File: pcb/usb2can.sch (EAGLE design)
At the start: 18 parts, among them IC1 ADM3053M, IC2 LD117AS33TR, K1 61400416021, K2 61900419521

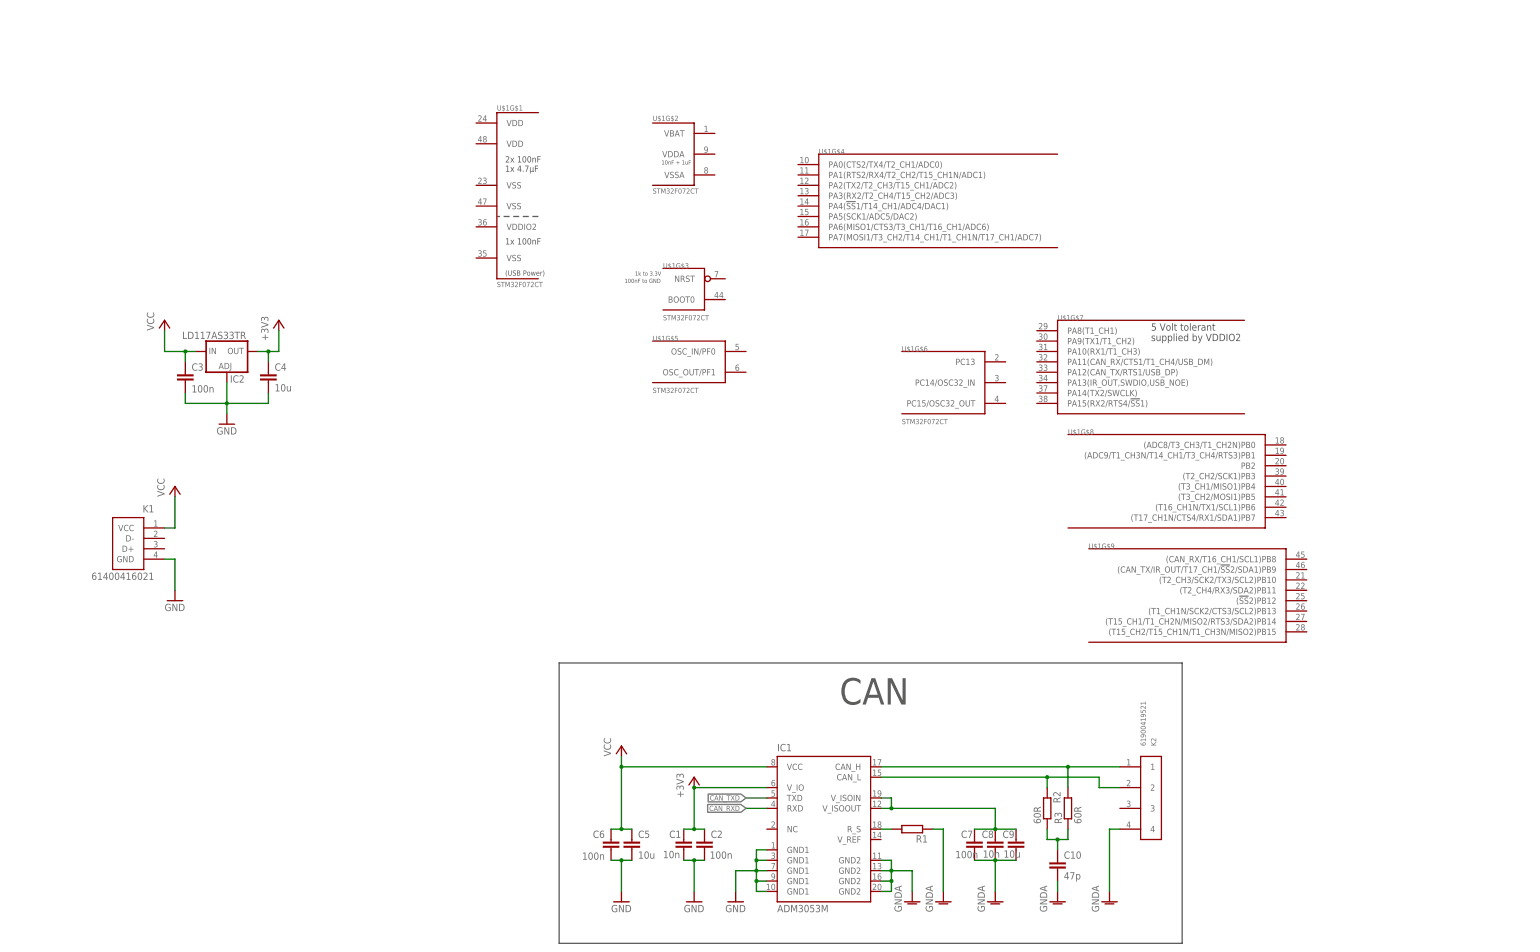
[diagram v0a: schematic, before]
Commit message: add some capacitors and connect USB and CAN
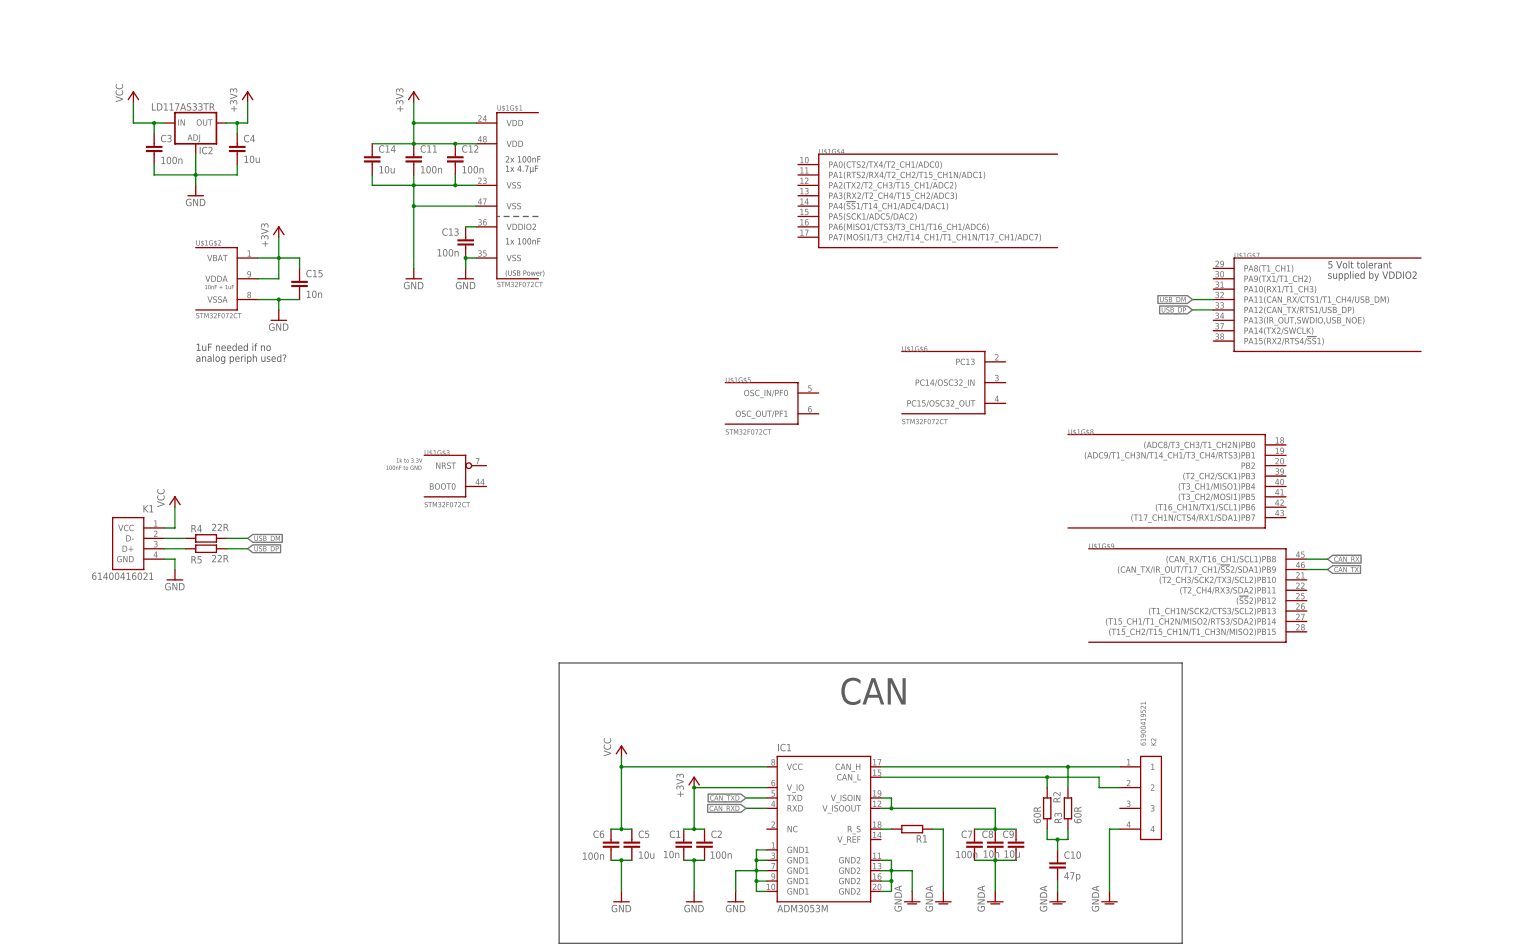
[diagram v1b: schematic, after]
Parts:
- added C11, C12, C13: 100n, rcl:C-EUC0603
- added C14: 10u, rcl:C-EUC0805K
- added C15: 10n, rcl:C-EUC0603
- added R4, R5: 22R, rcl:R-EU_R0805
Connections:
- new net CAN_RX: U$1G$9.(CAN_RX/T16_CH1/SCL1)PB8
- new net CAN_TX: U$1G$9.(CAN_TX/IR_OUT/T17_CH1/!SS!2/SDA1)PB9
- new net N$5: K1.D-, R4.1
- new net N$6: K1.D+, R5.1
- new net N$7: C13.1, U$1G$1.VDDIO2
- new net USB_DM: R4.2, U$1G$7.PA11(CAN_RX/CTS1/T1_CH4/USB_DM)
- new net USB_DP: R5.2, U$1G$7.PA12(CAN_TX/RTS1/USB_DP)
- net +3V3: now also C11.1, C12.1, C14.1, C15.1, U$1G$1.VDD@1, U$1G$1.VDD@2, U$1G$2.VBAT, U$1G$2.VDDA
- net GND: now also C11.2, C12.2, C13.2, C14.2, C15.2, U$1G$1.VSS@1, U$1G$1.VSS@2, U$1G$1.VSS@3, U$1G$2.VSSA
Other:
- note added: "1uF needed if no analog periph used?"
- moved on the sheet: C3, C4, IC2, U$1G$2, U$1G$3, U$1G$5, U$1G$7

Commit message: schematic: clock done, USB needs no series-R, debug port done, power supply revised
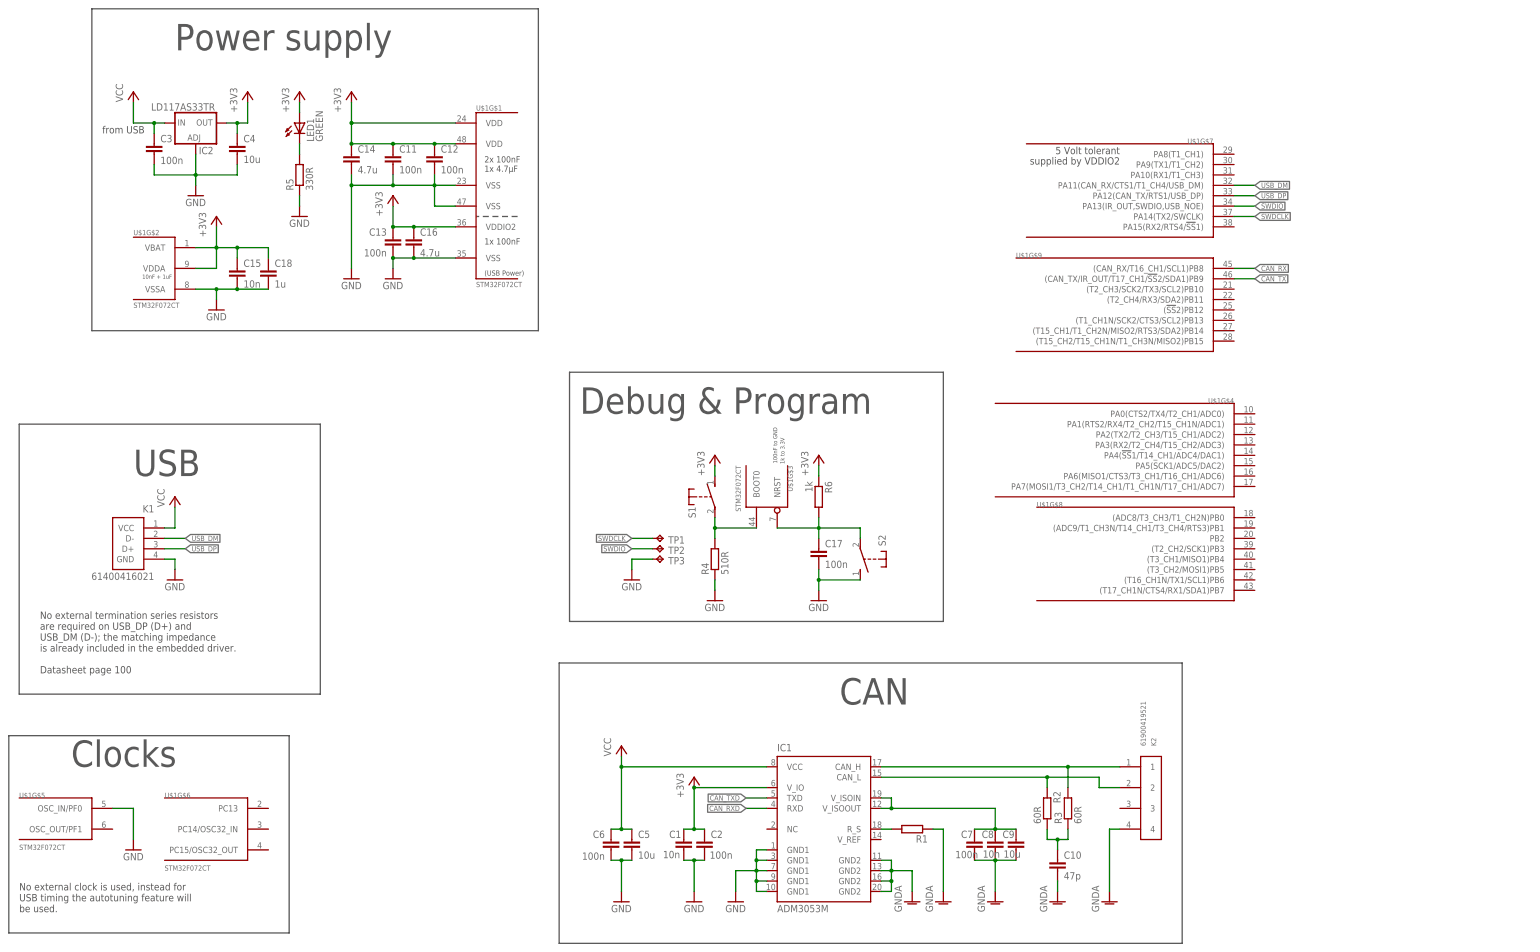
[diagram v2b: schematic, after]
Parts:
- added C16: 4.7u, rcl:C-EUC0805K
- added C17: 100n, rcl:C-EUC0603
- added C18: 1u, rcl:C-EUC0805K
- added LED1: GREEN, led:LEDCHIPLED_0603
- added R6: 1k, resistor:R-EU_R0603
- added S1, S2: MICRO_SWITCH_3X6X2.5S, micro_switch:MICRO_SWITCH_3X6X2.5S
- added TP1, TP2, TP3: TPB2,54, testpad:TPB2,54
- C14: value 10u -> 4.7u
- R4: value 22R -> 510R; device rcl:R-EU_R0805 -> resistor:R-EU_R0603
- R5: value 22R -> 330R; device rcl:R-EU_R0805 -> resistor:R-EU_R0603
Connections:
- new net SWDCLK: TP1.TP, U$1G$7.PA14(TX2/SWCLK)
- new net SWDIO: TP2.TP, U$1G$7.PA13(IR_OUT,SWDIO,USB_NOE)
- net +3V3: now also C13.1, C16.1, C18.1, LED1.A, R6.1, S1.1, U$1G$1.VDDIO2
- net GND: now also C16.2, C17.2, C18.2, R4.1, R5.1, S2.1, TP3.TP, U$1G$5.OSC_IN/PF0
- net N$5: now also LED1.C, R5.2; no longer K1.D-, R4.1
- net N$6: now also R4.2, S1.2, U$1G$3.BOOT0; no longer K1.D+, R5.1
- net N$7: now also C17.1, R6.2, S2.2, U$1G$3.NRST; no longer C13.1, U$1G$1.VDDIO2
- net USB_DM: now also K1.D-; no longer R4.2
- net USB_DP: now also K1.D+; no longer R5.2
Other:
- note added: "Clocks"
- note added: "Debug & Program"
- note added: "No external clock is used, instead for USB timing the autotuning feature will be used."
- note added: "No external termination series resistors are required on USB_DP (D+) and USB_DM (D-); the matching impedance is already included in the embedded driver. Datasheet page 100"
- note added: "Power supply"
- note added: "USB"
- note added: "from USB"
- note removed: "1uF needed if no analog periph used?"
- moved on the sheet: C11, C12, C13, C14, C15, R4, R5, U$1G$1, U$1G$2, U$1G$3, U$1G$4, U$1G$5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

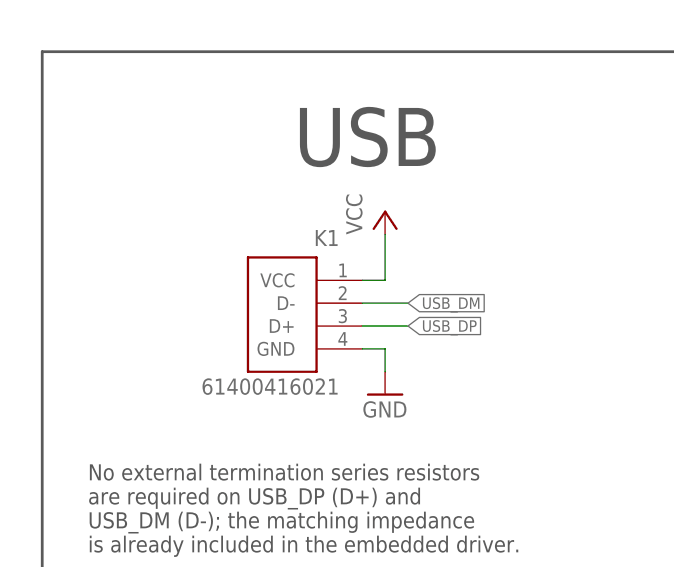
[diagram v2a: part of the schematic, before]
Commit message: schematic: use another usb connector and add forgotten library
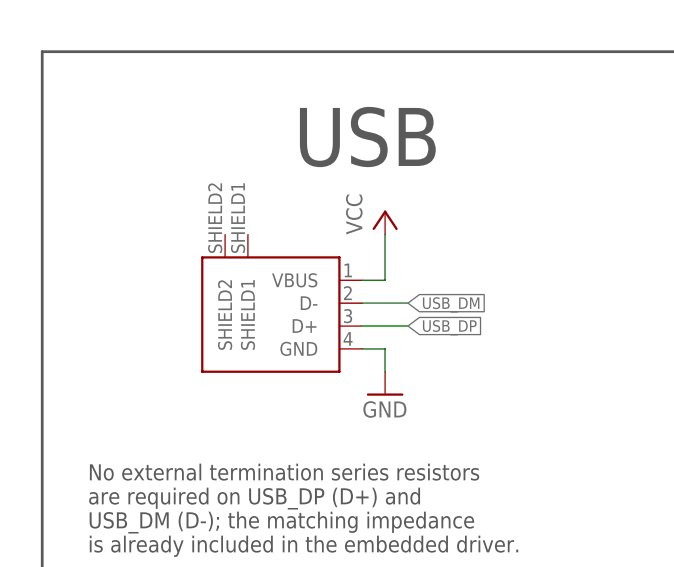
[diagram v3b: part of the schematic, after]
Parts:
- removed K1: 61400416021, Wuerth_Elektronik_eiCan_Communication_Connectors:61400416021
- added CON1: USB_A_MALESMD, micro_switch:USB_A_MALESMD
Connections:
- net GND: now also CON1.GND; no longer K1.GND
- net USB_DM: now also CON1.D-; no longer K1.D-
- net USB_DP: now also CON1.D+; no longer K1.D+
- net VCC: now also CON1.VBUS; no longer K1.VCC
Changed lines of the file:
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@@
 <part name="IC1" library="ADM3053" deviceset="ADM3053" device="M"/>
 <part name="GND1" library="supply1" deviceset="GND" device=""/>
-<part name="K1" library="Wuerth_Elektronik_eiCan_Communication_Connectors" deviceset="61400416021" device=""/>
 <part name="P+1" library="supply1" deviceset="VCC" device=""/>
 <part name="C1" library="rcl" deviceset="C-EU" device="C0603K" value="10n"/>
@@
 <part name="R5" library="resistor" deviceset="R-EU_" device="R0603" value="330R"/>
 <part name="GND18" library="supply1" deviceset="GND" device=""/>
+<part name="CON1" library="micro_switch" deviceset="USB_A_MALE" device="SMD"/>
 </parts>
 <sheets>
@@
 <instance part="IC1" gate="G$1" x="106.68" y="7.62"/>
 <instance part="GND1" gate="1" x="-53.34" y="68.58"/>
-<instance part="K1" gate="G$1" x="-66.04" y="78.74" rot="MR0"/>
 <instance part="P+1" gate="VCC" x="-53.34" y="88.9"/>
 <instance part="C1" gate="G$1" x="71.12" y="5.08" smashed="yes">
@@
 <instance part="R5" gate="G$1" x="-22.86" y="167.64" rot="R90"/>
 <instance part="GND18" gate="1" x="-22.86" y="157.48"/>
+<instance part="CON1" gate="G$1" x="-66.04" y="78.74"/>
 </instances>
 <busses>
@@
 <net name="VCC" class="0">
 <segment>
-<pinref part="K1" gate="G$1" pin="VCC"/>
 <wire x1="-55.88" y1="81.28" x2="-53.34" y2="81.28" width="0.1524" layer="91"/>
 <wire x1="-53.34" y1="81.28" x2="-53.34" y2="86.36" width="0.1524" layer="91"/>
 <pinref part="P+1" gate="VCC" pin="VCC"/>
+<pinref part="CON1" gate="G$1" pin="VBUS"/>
 </segment>
 <segment>
@@
 <net name="GND" class="0">
 <segment>
-<pinref part="K1" gate="G$1" pin="GND"/>
 <wire x1="-55.88" y1="73.66" x2="-53.34" y2="73.66" width="0.1524" layer="91"/>
 <wire x1="-53.34" y1="73.66" x2="-53.34" y2="71.12" width="0.1524" layer="91"/>
 <pinref part="GND1" gate="1" pin="GND"/>
+<pinref part="CON1" gate="G$1" pin="GND"/>
 </segment>
 <segment>
@@
 <segment>
 <label x="-50.8" y="78.74" size="1.27" layer="95" xref="yes"/>
-<pinref part="K1" gate="G$1" pin="D-"/>
 <wire x1="-55.88" y1="78.74" x2="-50.8" y2="78.74" width="0.1524" layer="91"/>
+<pinref part="CON1" gate="G$1" pin="D-"/>
 </segment>
 </net>
@@
 <segment>
 <label x="-50.8" y="76.2" size="1.27" layer="95" xref="yes"/>
-<pinref part="K1" gate="G$1" pin="D+"/>
 <wire x1="-50.8" y1="76.2" x2="-55.88" y2="76.2" width="0.1524" layer="91"/>
-</segment>
-</net>
+<pinref part="CON1" gate="G$1" pin="D+"/>
+</segment>
+</net>
